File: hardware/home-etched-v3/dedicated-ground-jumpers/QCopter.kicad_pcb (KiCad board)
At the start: 2 copper layers, 92 x 82 mm, 12 parts, among them J1 LIDAR_SOLDER_WIRES, J2 ESC_Servo_1x03, J3 ESC_Servo_1x03, J4 ESC_Servo_1x03, J5 ESC_Servo_1x03, U1 ESP32_S3_DevKitC_1_44pin, U2 MPU6050_GY521_1x08, U3 BMP280_GY_1x06, U4 Magnetometer_GY271_1x05

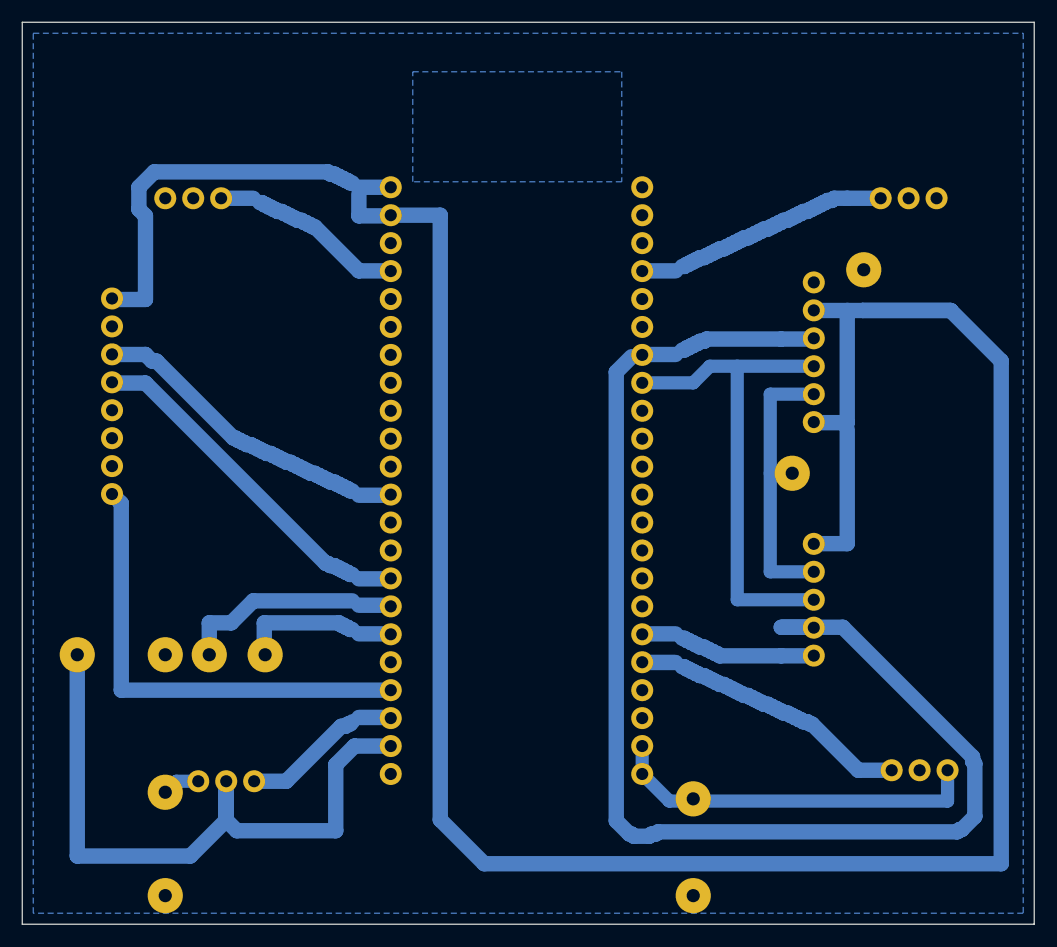
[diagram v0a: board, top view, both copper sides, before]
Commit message: Clear antenna-edge copper and preserve common ground with three wire links
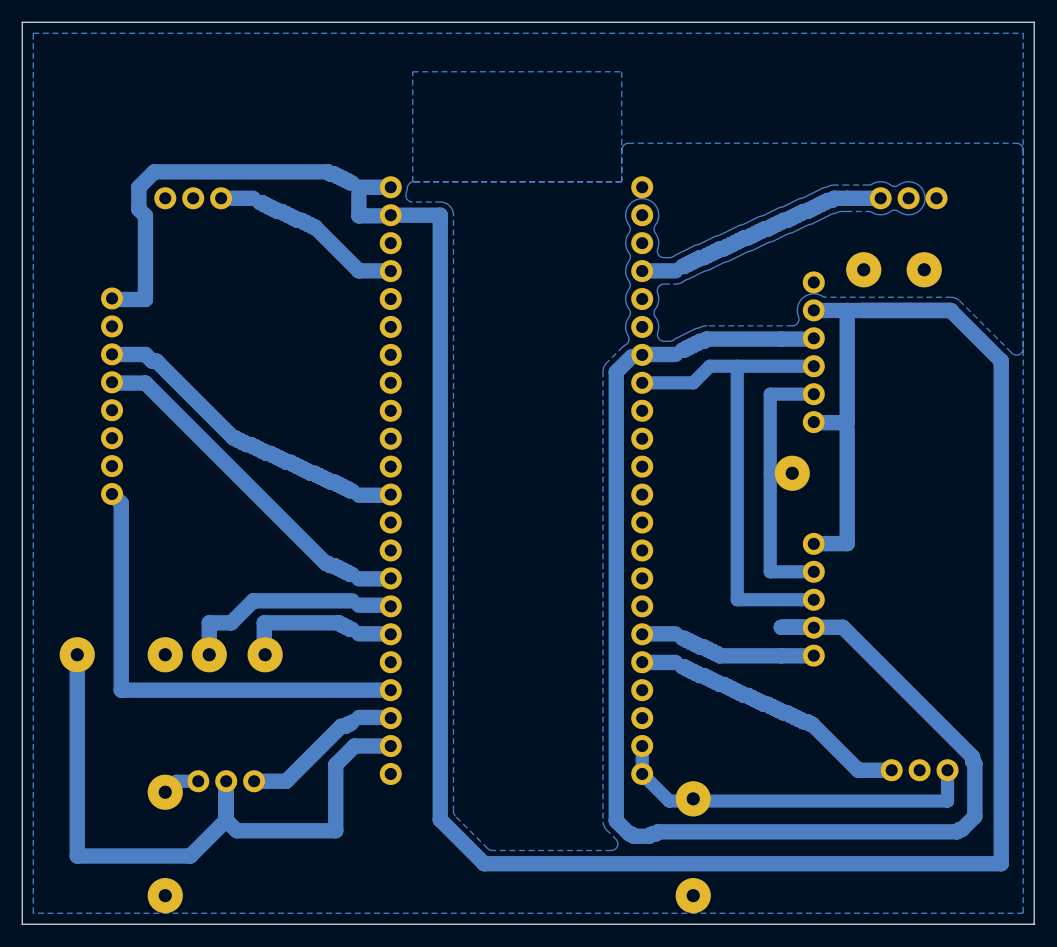
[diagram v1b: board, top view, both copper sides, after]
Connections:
- G1 pad 2: GND -> GND_RF_RETURN
- J2 pad 1: GND -> GND_RF_RETURN
- U1 pad 44: GND -> GND_RF_RETURN
- U3 pad 6: GND -> GND_RF_RETURN
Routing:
- added copper zone on B.Cu, net GND_RF_RETURN
